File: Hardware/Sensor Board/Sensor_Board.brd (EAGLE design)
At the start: 100 x 80 mm, 13 parts, among them Q1 MMBT2222A

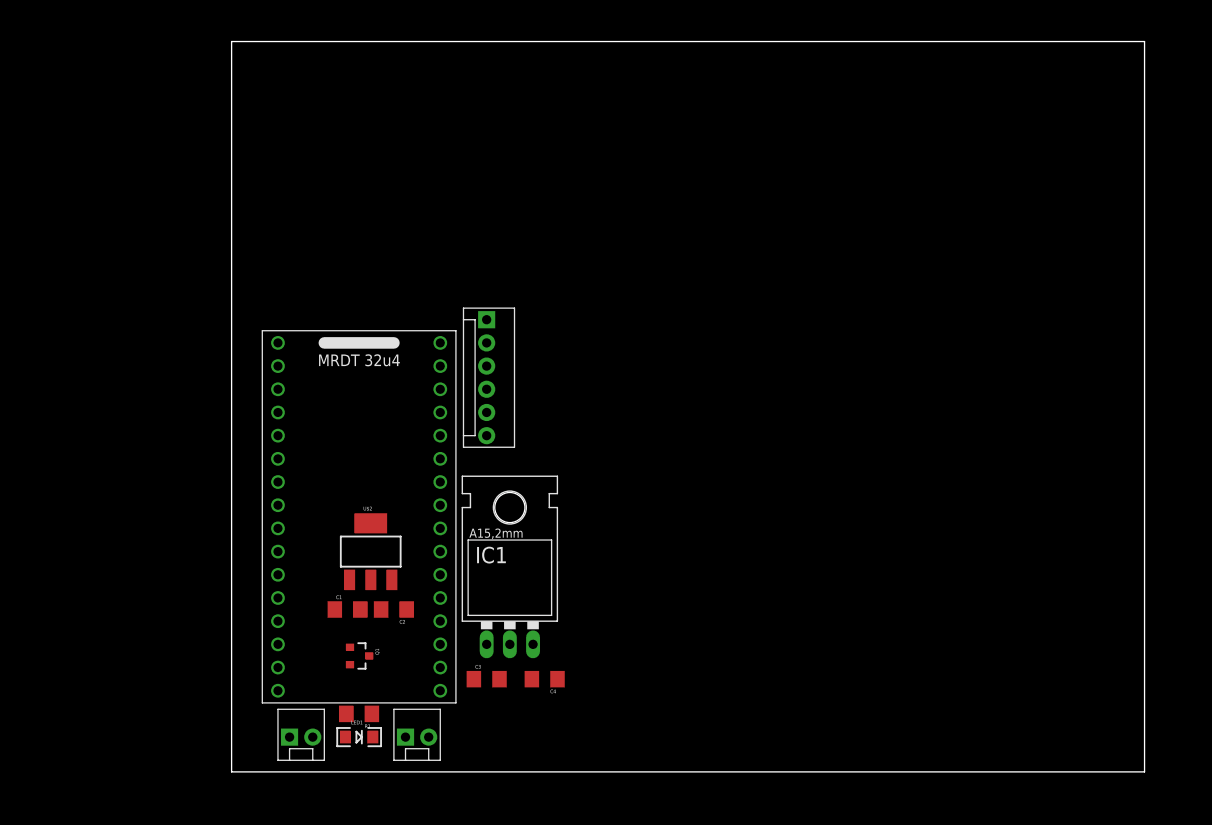
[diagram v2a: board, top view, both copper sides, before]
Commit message: added crystal
and moisture sensor
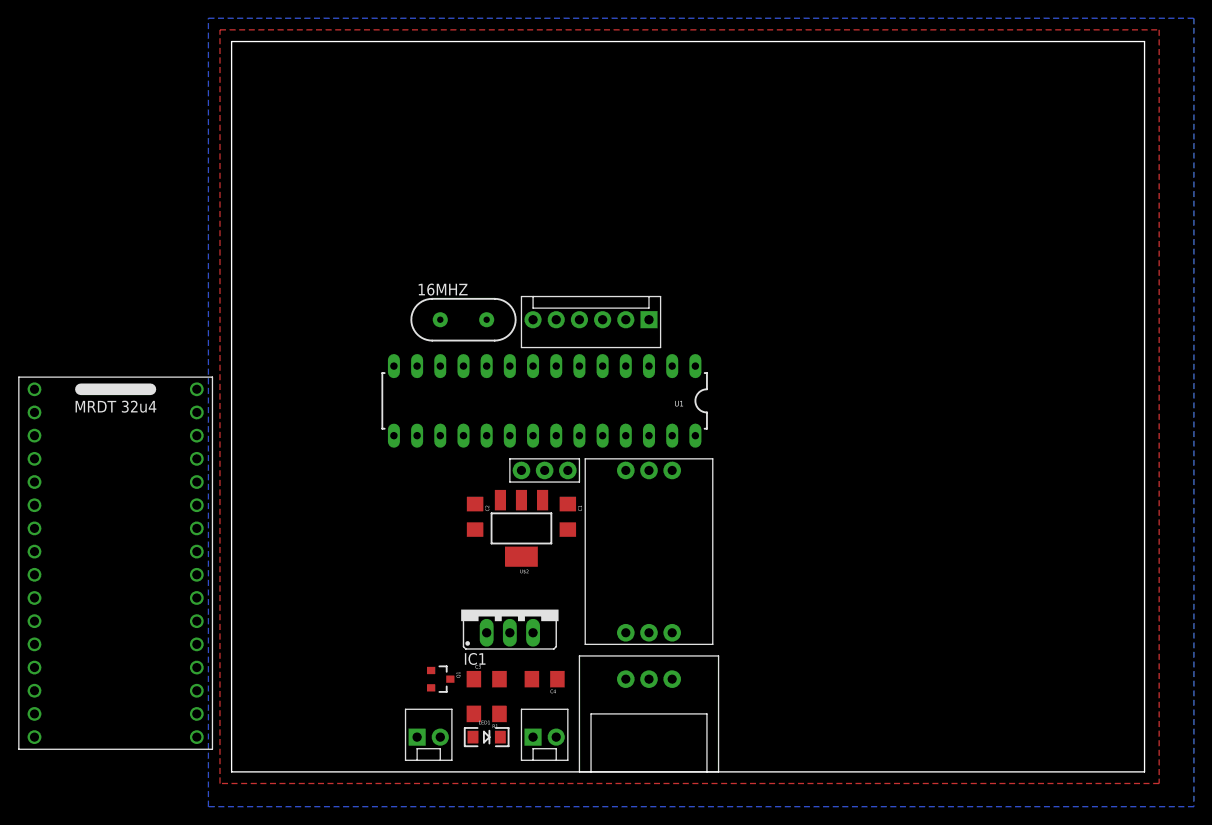
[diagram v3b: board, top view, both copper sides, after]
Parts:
- added 16MHZ: (no value), SparkFun-FreqCtrl:HC49US
- added U$3: PH_EZ0, pH_EZ0:PH_EZ0
- added U$4: PH_CONNECTOR, PH_CONNECTOR:PH_CONNECTOR
- added U$5: MOISTURE_SENSOR, moisture sensor:MOISTURE_SENSOR
- added U1: ATMEGA328P_PDIP, SparkFun-DigitalIC:DIL28-3
- IC1: device v-reg:78XXL -> v-reg:78XXS
- moved U$1 27.1 mm to (-12.7, 22.9)
- moved C1 26.2 mm to (36.8, 27.9), turned to 270 degrees
- moved JP1 17.8 mm to (45.7, 49.5), turned to 180 degrees
- moved U$2 16.7 mm to (31.8, 26.7), turned to 180 degrees
- moved JP2 14.0 mm to (33.0, 3.81)
- moved JP3 14.0 mm to (20.3, 3.81)
- moved LED1 14.0 mm to (27.9, 3.81)
- moved R1 14.0 mm to (27.9, 6.35)
- moved C2 13.5 mm to (26.7, 27.9), turned to 270 degrees
- moved Q1 9.25 mm to (22.9, 10.2)
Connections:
- removed net N$11: U$1.28
- new net MOIS_SENSOR: U$5.I_AN, U1.14, U1.23
- new net N$1: 16MHZ.2, U1.9
- new net N$4: 16MHZ.1, U1.10
- new net N$5: U$3.PRB, U$4.PRB
- new net RX: U$3.RX, U1.2
- new net TX: U$3.TX, U1.3
- net 3.3V: now also U1.20, U1.21, U1.7; no longer U$1.18
- net 5V: now also U$3.VCC, U$4.VCC, U$5.VCC
- net GND: now also U$3.GND, U$3.PGND, U$4.GND, U$5.GND, U1.22, U1.8; no longer U$1.15, U$1.17
- net ICG: now also U1.4; no longer U$1.32
- net SH: now also U1.5; no longer U$1.30
- net TRANS_LASER: now also U1.13; no longer U$1.13
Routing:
- added copper zone on layer 1, net 5V
- added copper zone on layer 16, net GND

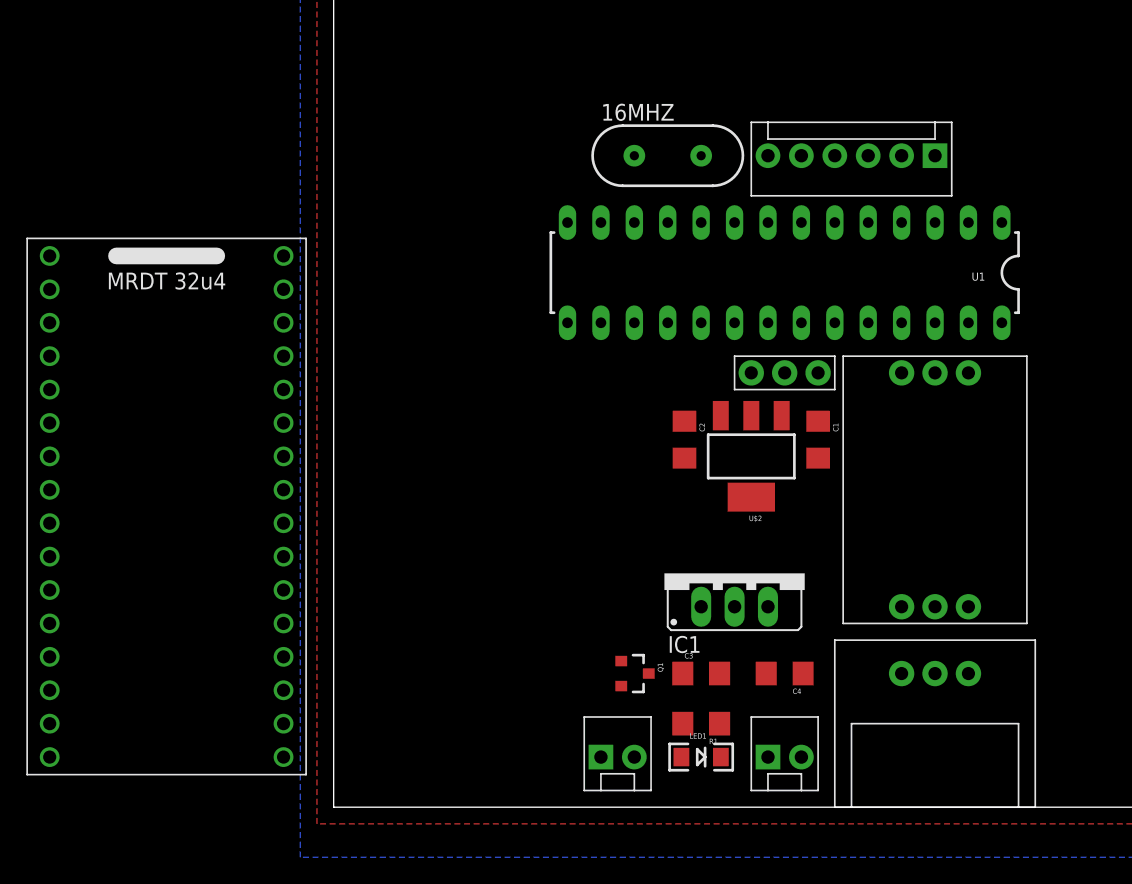
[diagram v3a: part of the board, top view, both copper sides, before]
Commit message: updated the board
most wires have been checked. Not all wires are in.
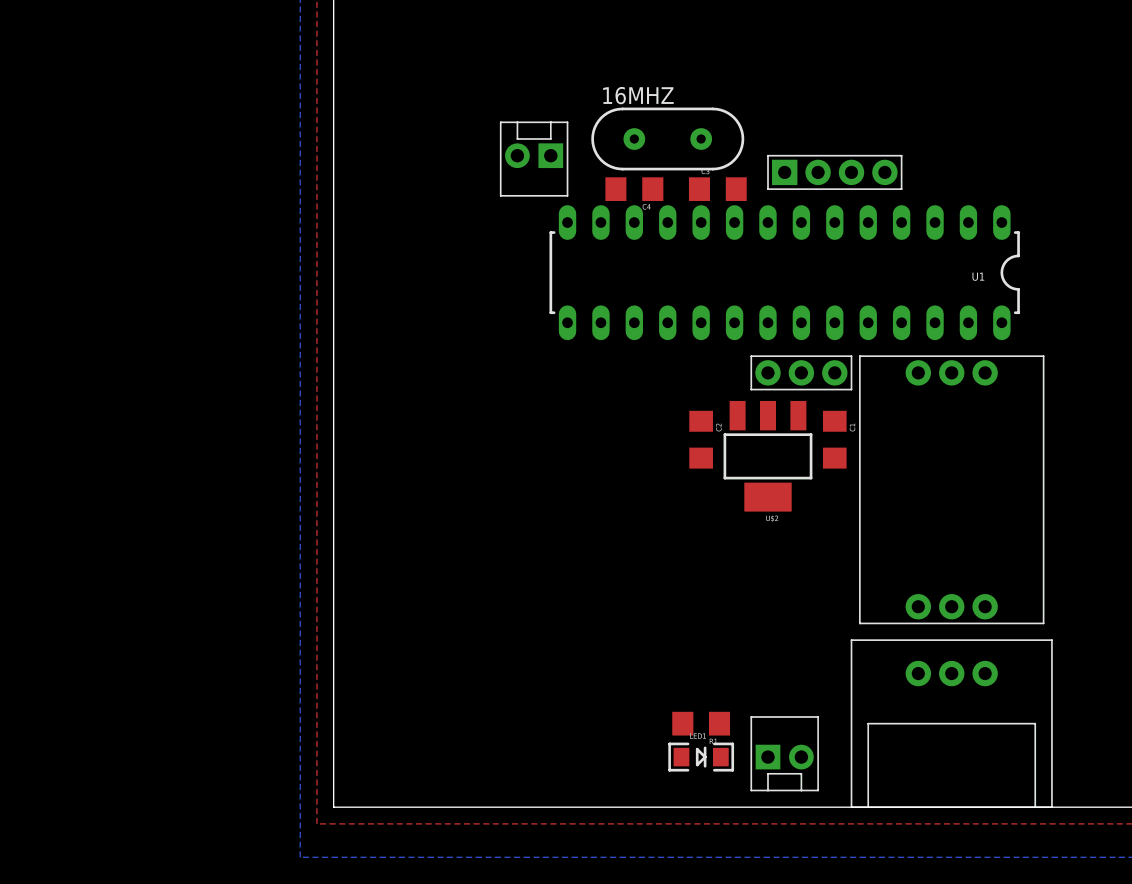
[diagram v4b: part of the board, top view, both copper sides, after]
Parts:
- removed IC1: (no value), v-reg:78XXS
- removed JP1: (no value), SparkFun-Connectors:MOLEX-1X6
- removed Q1: MMBT2222A, SparkFun-DiscreteSemi:SOT23-3
- removed U$1: 32U4_BREAKOUT, MRDT-2015-General:32U4_MCU_DIP
- added U$6: CCD_CONNECTOR, CCD_CONNECTOR:CCD_CONNECTOR
- C3, C4: value .1uF -> (none)
- moved JP3 45.9 mm to (16.5, 49.5), turned to 180 degrees
- moved C4 38.6 mm to (22.9, 47.0)
- moved C3 36.9 mm to (29.2, 47.0)
- moved C1 1.27 mm to (38.1, 27.9)
- moved U$2 1.27 mm to (33.0, 26.7)
- moved U$3 1.27 mm to (40.0, 14.0)
- moved U$4 1.27 mm to (47.0, 7.62)
- moved U$5 1.27 mm to (35.6, 33.0)
- moved C2 1.27 mm to (27.9, 27.9)
- moved 16MHZ 1.27 mm to (25.4, 50.8)
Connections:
- removed net ICG: JP1.2, U1.4
- removed net M: JP1.3, U$1.31
- removed net N$1: 16MHZ.2, U1.9
- removed net N$7: JP3.2, Q1.2
- removed net OS: JP1.5, U$1.29
- removed net SH: JP1.4, U1.5
- removed net TRANS_LASER: Q1.1, U1.13
- new net CCD_RX: U$6.TX, U1.6
- new net CCD_TX: U$6.RX, U1.11
- new net LASER_CTR: U1.12
- new net N$2: 16MHZ.2, C3.1, U1.9
- new net TO_LAZER: JP3.2
- new net TO_MOSFET: JP3.1
- net 3.3V: no longer C3.1, IC1.IN, Q1.3
- net 5V: now also U$6.5V; no longer C4.1, IC1.OUT, JP1.1
- net GND: now also U$6.GND; no longer IC1.GND, JP1.6, JP3.1
- net MOIS_SENSOR: no longer U1.14
- net N$4: now also C4.1
- net RX: now also U1.4; no longer U1.2
- net TX: now also U1.5; no longer U1.3
